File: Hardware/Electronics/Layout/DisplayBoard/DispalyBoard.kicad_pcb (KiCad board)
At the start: 2 copper layers, 91.8 x 91.6 mm, 153 parts, among them P1 CONN_02X08, Q1 TSM3401, Q10 TSM3401, Q11 TSM3401, Q12 TSM3401, Q13 TSM3401, Q14 TSM3401, Q15 TSM3401, Q16 TSM3401, Q17 TSM3401, Q18 TSM3401, Q19 TSM3401, Q2 TSM3401, Q20 TSM3401, Q21 TSM3401, Q22 TSM3401, Q23 TSM3401, Q24 TSM3401, Q25 TSM3401, Q26 TSM3401, Q27 TSM3401, Q28 TSM3401, Q29 TSM3401, Q3 TSM3401, Q30 TSM3401, Q31 TSM3401, Q32 TSM3401, Q4 TSM3401, Q5 TSM3401, Q6 TSM3401, Q7 TSM3401, Q8 TSM3401, Q9 TSM3401, U1 TLC59208F, U2 TLC59208F, U3 TLC59208F, U4 TLC59208F, U5 74HC595, U6 74HC595, U7 74HC595, U8 74HC595

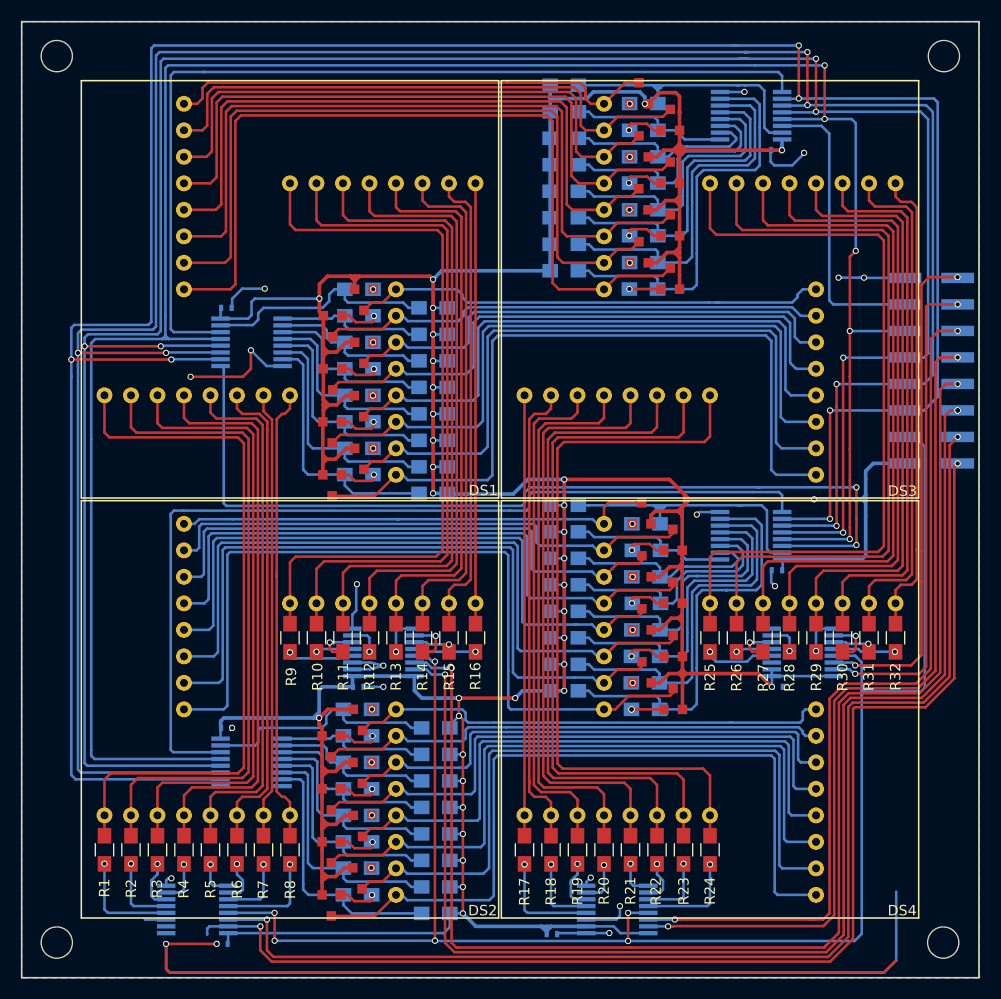
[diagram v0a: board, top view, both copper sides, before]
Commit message: Changed dispaly board schematic and layout version to 1.0.0 Moved vias from the capacitor pads Added github link on the silkscreen Changed files architecture Pushed new gerbers
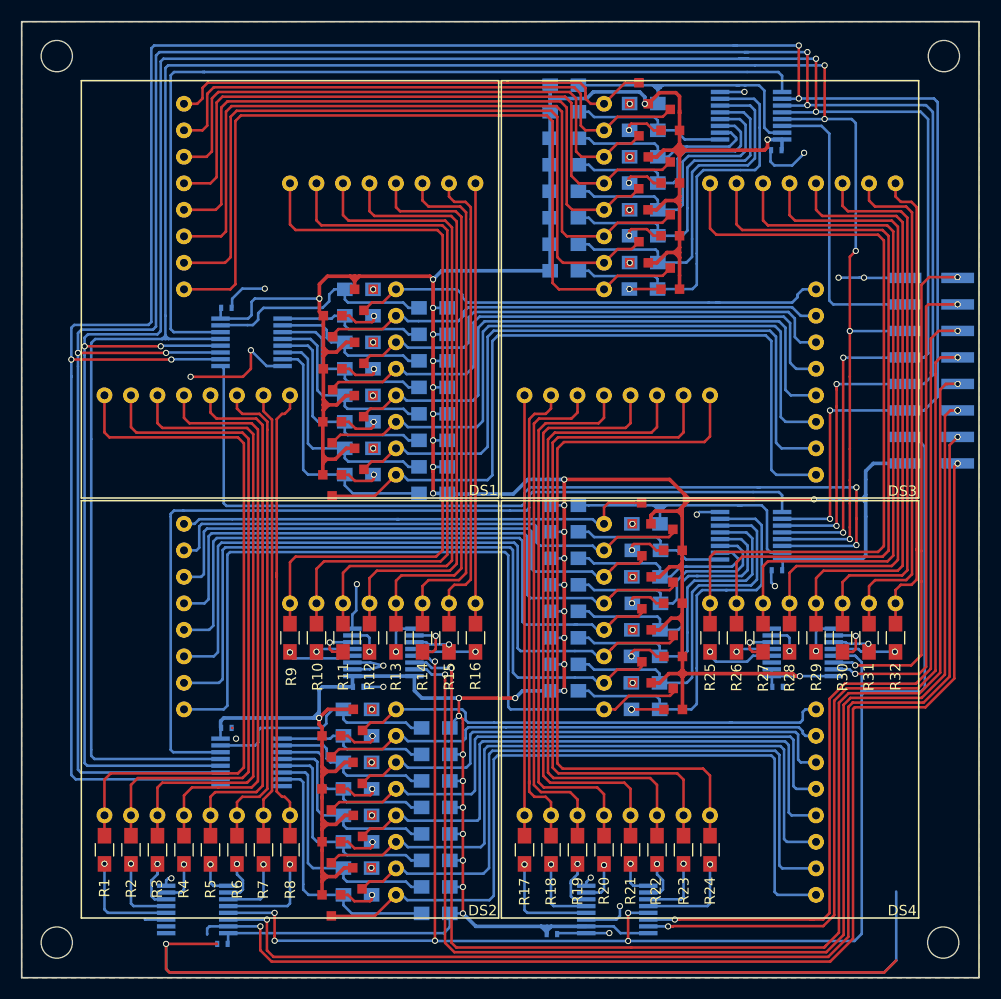
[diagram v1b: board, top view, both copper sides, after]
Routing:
- net +3V3: track 593.3 -> 596.8 mm
- net GND: vias 19 -> 18
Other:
- board text added: "Wooden Clock github.com/ProrokWielki/Wooden-Clock Display board v.1.0.0 Paweł Warzecha pawel.warzecha@yahoo.com"
- board text removed: "Wooden Clock Display board v.0.2.1 Paweł Warzecha pawel.warzecha@yahoo.com"
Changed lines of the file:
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@@
     (thickness 1.6)
     (drawings 22)
-    (tracks 2413)
+    (tracks 2418)
     (zones 0)
     (modules 153)
@@
   )
   (layers
-    (0 F.Cu signal hide)
+    (0 F.Cu signal)
     (31 B.Cu signal)
     (32 B.Adhes user)
@@
     (visible_elements 7FFFFF7F)
     (pcbplotparams
-      (layerselection 0x010f0_80000001)
+      (layerselection 0x010f0_ffffffff)
       (usegerberextensions false)
       (usegerberattributes false)
@@
       (drillshape 0)
       (scaleselection 1)
-      (outputdirectory ""))
+      (outputdirectory "Gerber/"))
   )
   (net 0 "")
@@
     (pad 1 np_thru_hole circle (at 0 0) (size 3 3) (drill 3) (layers *.Cu *.Mask))
   )
-  (gr_text "Wooden Clock\nDisplay board v.0.2.1\nPaweł Warzecha\npawel.warzecha@yahoo.com\n" (at 110.0836 91.44 90) (layer B.SilkS)
+  (gr_text "Wooden Clock\ngithub.com/ProrokWielki/Wooden-Clock\nDisplay board v.1.0.0\nPaweł Warzecha\npawel.warzecha@yahoo.com" (at 110.0709 89.8906 90) (layer B.SilkS)
     (effects (font (size 1.5 1.5) (thickness 0.3)) (justify left mirror))
   )
@@
   (segment (start 183.4475 98.9965) (end 183.4475 96.905) (width 0.35) (layer B.Cu) (net 1))
   (segment (start 178.4985 97.3455) (end 183.4475 97.3455) (width 0.35) (layer B.Cu) (net 1))
-  (segment (start 173.186 114.046) (end 174.456 115.316) (width 0.35) (layer F.Cu) (net 1))
   (segment (start 153.209 115.697) (end 154.559 115.697) (width 0.35) (layer B.Cu) (net 1))
   (segment (start 149.86 116.3955) (end 150.5585 115.697) (width 0.35) (layer B.Cu) (net 1))
@@
   (segment (start 183.4475 97.3455) (end 183.4475 97.028) (width 0.25) (layer B.Cu) (net 1))
   (segment (start 183.4475 97.028) (end 183.4475 95.4445) (width 0.25) (layer B.Cu) (net 1))
-  (via (at 174.456 115.316) (size 0.6) (drill 0.4) (layers F.Cu B.Cu) (net 1))
+  (via (at 177.1396 114.3) (size 0.6) (drill 0.4) (layers F.Cu B.Cu) (net 1))
   (segment (start 174.456 114.29864) (end 174.456 115.316) (width 0.25) (layer B.Cu) (net 1))
   (segment (start 174.44466 114.2873) (end 180.39334 114.2873) (width 0.25) (layer B.Cu) (net 1))
@@
   (segment (start 165.8874 113.6904) (end 165.8874 113.7158) (width 0.35) (layer F.Cu) (net 1))
   (segment (start 166.2176 114.046) (end 165.8874 114.046) (width 0.35) (layer F.Cu) (net 1))
-  (segment (start 173.186 114.046) (end 166.2176 114.046) (width 0.35) (layer F.Cu) (net 1))
   (segment (start 165.8874 113.6904) (end 165.8874 114.046) (width 0.35) (layer F.Cu) (net 1))
   (segment (start 165.8874 112.40516) (end 165.8874 113.6904) (width 0.35) (layer F.Cu) (net 1))
@@
   (segment (start 161.782602 58.293) (end 162.275198 58.785596) (width 0.35) (layer B.Cu) (net 1))
   (segment (start 157.353 58.293) (end 161.782602 58.293) (width 0.35) (layer B.Cu) (net 1))
-  (via (at 175.429 63.881) (size 0.6) (drill 0.4) (layers F.Cu B.Cu) (net 1))
+  (via (at 174.0408 62.865) (size 0.6) (drill 0.4) (layers F.Cu B.Cu) (net 1))
   (segment (start 165.608 63.3222) (end 165.608 61.98616) (width 0.35) (layer F.Cu) (net 1))
-  (segment (start 175.429 63.881) (end 166.1668 63.881) (width 0.35) (layer F.Cu) (net 1))
   (segment (start 166.1668 63.881) (end 165.608 63.3222) (width 0.35) (layer F.Cu) (net 1))
   (segment (start 165.608 75.884402) (end 165.608 77.20076) (width 0.35) (layer F.Cu) (net 1))
@@
   (segment (start 146.08556 138.27506) (end 144.8435 137.033) (width 0.35) (layer B.Cu) (net 1))
   (segment (start 156.66466 138.27506) (end 146.08556 138.27506) (width 0.35) (layer B.Cu) (net 1))
+  (segment (start 172.9232 63.881) (end 166.1668 63.881) (width 0.35) (layer F.Cu) (net 1))
+  (segment (start 176.461336 114.046) (end 165.8874 114.046) (width 0.35) (layer F.Cu) (net 1))
+  (segment (start 176.715336 114.3) (end 176.461336 114.046) (width 0.35) (layer F.Cu) (net 1))
+  (segment (start 177.1396 114.3) (end 176.715336 114.3) (width 0.35) (layer F.Cu) (net 1))
+  (segment (start 173.7487 63.881) (end 172.9232 63.881) (width 0.35) (layer F.Cu) (net 1))
+  (segment (start 174.0408 63.5889) (end 173.7487 63.881) (width 0.35) (layer F.Cu) (net 1))
+  (segment (start 174.0408 62.865) (end 174.0408 63.5889) (width 0.35) (layer F.Cu) (net 1))
+  (segment (start 175.42764 62.865) (end 175.44034 62.8523) (width 0.35) (layer B.Cu) (net 1))
+  (segment (start 174.0408 62.865) (end 175.42764 62.865) (width 0.35) (layer B.Cu) (net 1))
   (segment (start 116.3955 139.954) (end 116.3955 142.367) (width 0.25) (layer F.Cu) (net 2))
   (segment (start 185.2295 142.6845) (end 186.3725 141.5415) (width 0.25) (layer F.Cu) (net 2))
@@
   (segment (start 116.3955 139.954) (end 121.243 139.954) (width 0.25) (layer F.Cu) (net 2))
   (segment (start 121.2215 139.954) (end 121.243 139.954) (width 0.25) (layer F.Cu) (net 2))
-  (via (at 121.243 139.954) (size 0.6) (drill 0.4) (layers F.Cu B.Cu) (net 2))
   (via (at 116.3955 139.954) (size 0.6) (drill 0.4) (layers F.Cu B.Cu) (net 2))
   (segment (start 116.3955 139.954) (end 116.3955 142.367) (width 0.25) (layer B.Cu) (net 2))
@@
   (via (at 171.831 58.293) (size 0.6) (drill 0.4) (layers F.Cu B.Cu) (net 2))
   (segment (start 171.8183 58.3057) (end 171.831 58.293) (width 0.25) (layer B.Cu) (net 2))
-  (via (at 122.724 119.253) (size 0.6) (drill 0.4) (layers F.Cu B.Cu) (net 2))
+  (via (at 123.1011 120.2817) (size 0.6) (drill 0.4) (layers F.Cu B.Cu) (net 2))
   (segment (start 122.724 119.253) (end 122.7455 119.253) (width 0.25) (layer F.Cu) (net 2))
   (segment (start 135.3605 115.316) (end 137.2235 115.316) (width 0.25) (layer B.Cu) (net 2))

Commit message: updated schematics
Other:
- net class 1A removed
- net class Default removed
